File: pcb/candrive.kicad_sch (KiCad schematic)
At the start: 64 parts, among them J1 Conn_01x02_Male, J2 Conn_01x06_Male, J3 Conn_01x06_Male, J4 Conn_01x06_Male, J5 Conn_01x03_Male, J6 Conn_01x06_Male, Q1 AO3401A, Q2 BC546, SW1 SW_Push, U1 STM32F103RBTx, U2 LD1117S33TR_SOT223, U3 SN65HVD234, U6 MAX5035BUSA

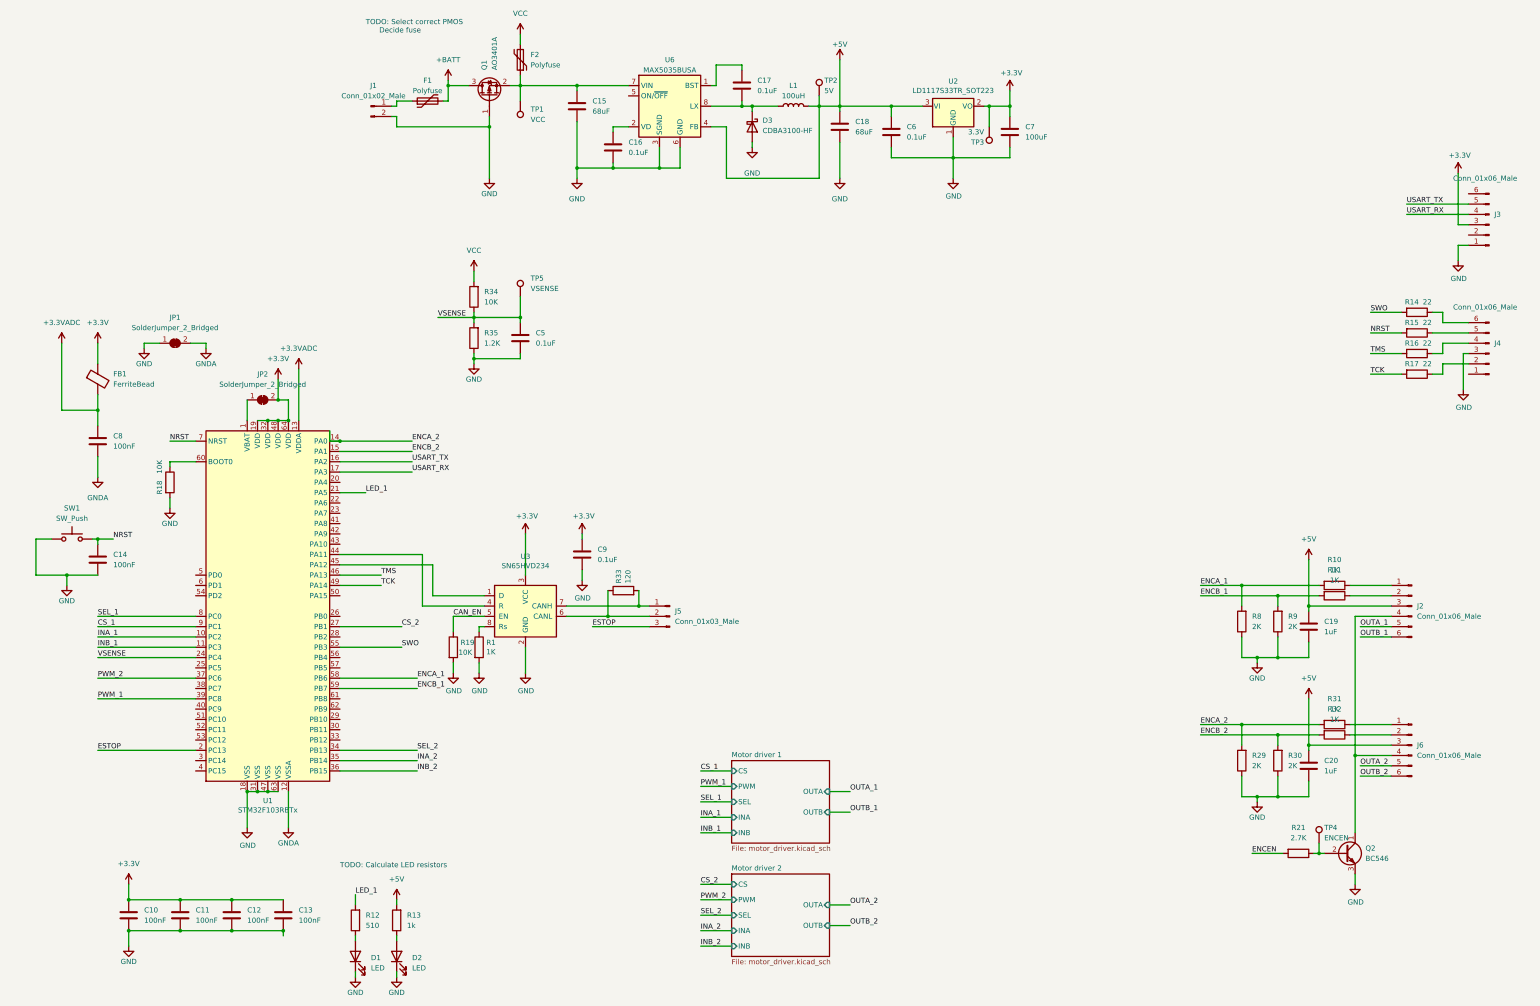
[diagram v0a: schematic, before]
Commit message: Fix some ERC warnings
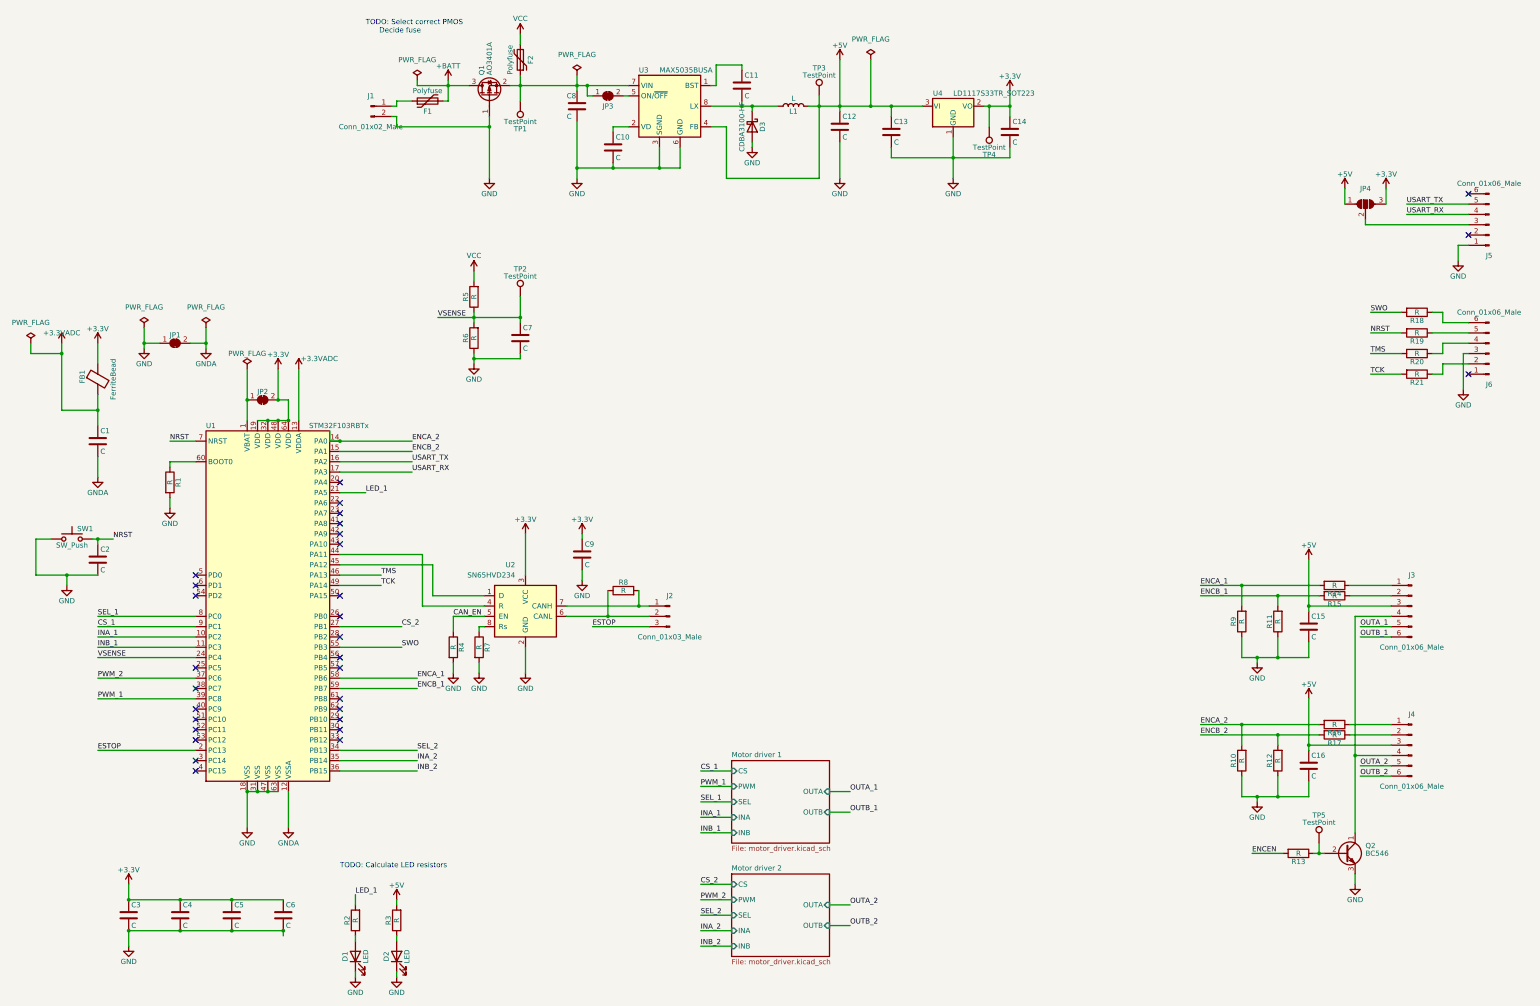
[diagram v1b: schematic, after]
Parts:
- added JP3: SolderJumper_2_Bridged, Jumper:SolderJumper-2_P1.3mm_Open_TrianglePad1.0x1.5mm, symbol Jumper:SolderJumper_2_Bridged
- added JP4: SolderJumper_3_Open, symbol Jumper:SolderJumper_3_Open
- C1: renamed from C8; value 100nF -> C
- C10: renamed from C16; value 0.1uF -> C
- C11: renamed from C17; value 0.1uF -> C
- C12: renamed from C18; value 68uF -> C
- C13: renamed from C6; value 0.1uF -> C
- C14: renamed from C7; value 100uF -> C
- C15: renamed from C19; value 1uF -> C
- C16: renamed from C20; value 1uF -> C
- C2: renamed from C14; value 100nF -> C
- C3: renamed from C10; value 100nF -> C
- C4: renamed from C11; value 100nF -> C
- C5: renamed from C12; value 100nF -> C
- C6: renamed from C13; value 100nF -> C
- C7: renamed from C5; value 0.1uF -> C
- C8: renamed from C15; value 68uF -> C
- C9: value 0.1uF -> C
- JP2: now left out of the parts list
- L1: value 100uH -> L
- R1: renamed from R18; value 10K -> R
- R10: renamed from R29; value 2K -> R
- R11: renamed from R9; value 2K -> R
- R12: renamed from R30; value 2K -> R
- R13: renamed from R21; value 2.7K -> R
- R14: renamed from R10; value 1K -> R
- R15: renamed from R11; value 1K -> R
- R16: renamed from R31; value 1K -> R
- R17: renamed from R32; value 1K -> R
- R18: renamed from R14; value 22 -> R
- R19: renamed from R15; value 22 -> R
- R2: renamed from R12; value 510 -> R
- R20: renamed from R16; value 22 -> R
- R21: renamed from R17; value 22 -> R
- R3: renamed from R13; value 1k -> R
- R4: renamed from R19; value 10K -> R
- R5: renamed from R34; value 10K -> R
- R6: renamed from R35; value 1.2K -> R
- R7: renamed from R1; value 1K -> R
- R8: renamed from R33; value 120 -> R
- R9: renamed from R8; value 2K -> R
- TP1: value VCC -> TestPoint
- TP2: renamed from TP5; value VSENSE -> TestPoint
- TP3: renamed from TP2; value 5V -> TestPoint
- TP4: renamed from TP3; value 3.3V -> TestPoint
- TP5: renamed from TP4; value ENCEN -> TestPoint
- renumbered J5 to J2, J2 to J3, J6 to J4, J3 to J5, J4 to J6, U3 to U2, U6 to U3, U2 to U4
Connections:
- net +5V: now also JP4.1 (A)
- net at C8.1, F2.1, Q1.2 (S)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: now also JP3.1 (A)
- net at U3.5 (ON/~{OFF}): now also JP3.2 (B)
- net +3V3 renamed +3.3V
- net +3.3V: now also JP4.3 (B); no longer J5.3 (Pin_3)
- new net: J5.3 (Pin_3), JP4.2 (C)
- no-connect marks 0 -> 30

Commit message: Replace VNH7070BAS with TLE7209 in schematic
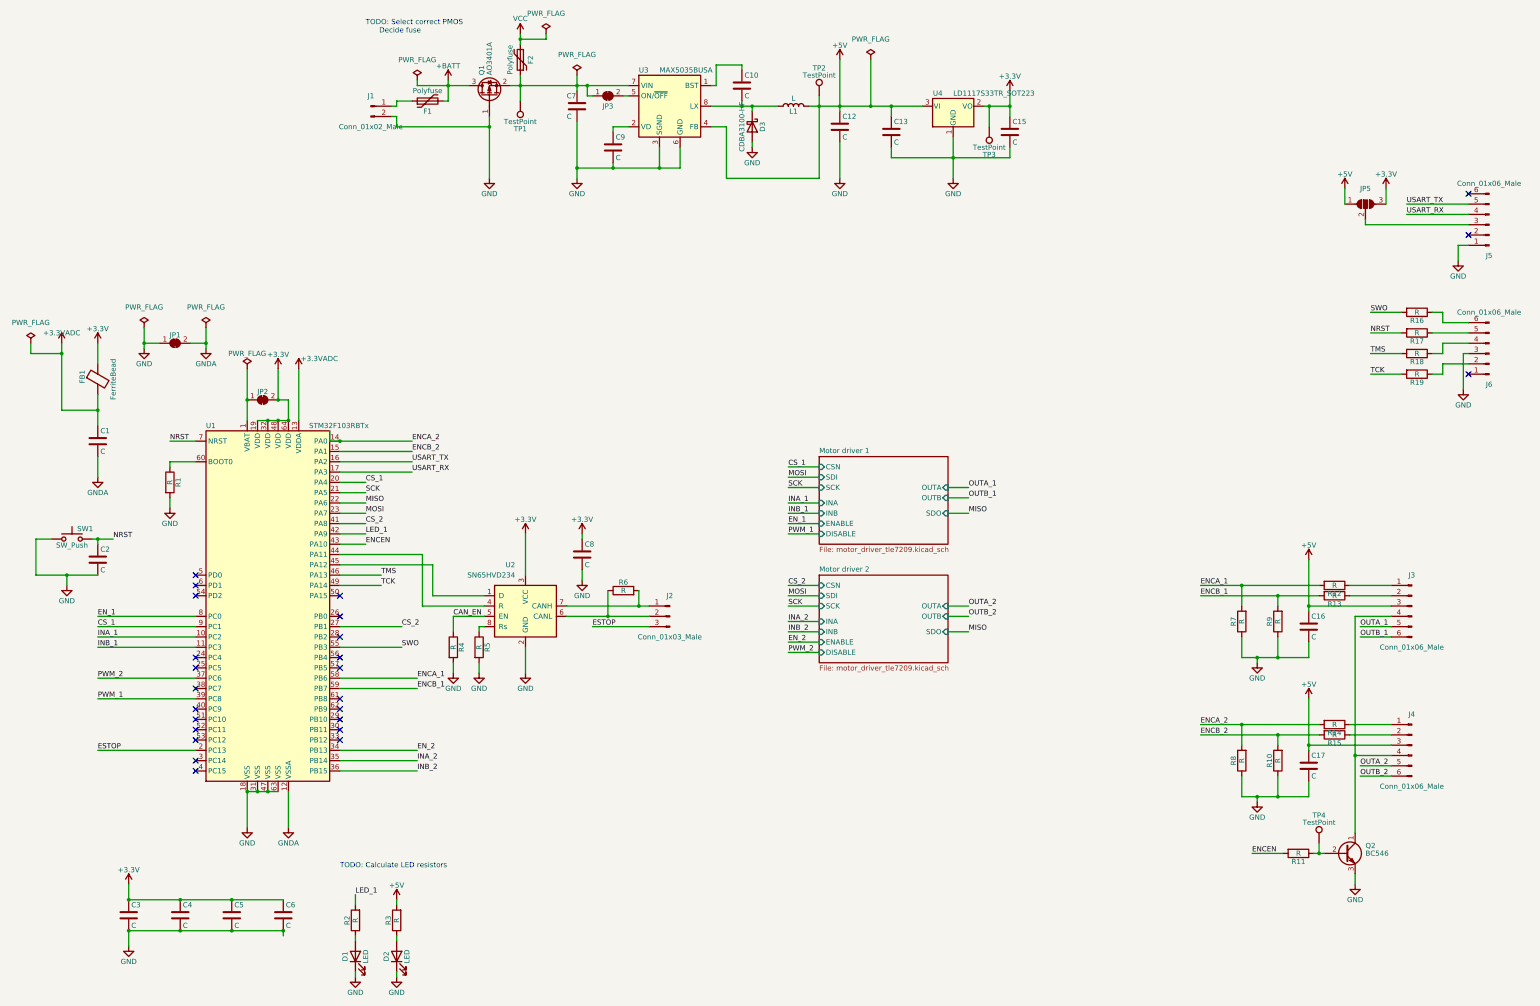
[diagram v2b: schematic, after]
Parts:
- removed C7: C, Capacitor_SMD:C_0805_2012Metric_Pad1.18x1.45mm_HandSolder, symbol Device:C
- removed R5, R6: R, Resistor_SMD:R_0805_2012Metric_Pad1.20x1.40mm_HandSolder, symbol Device:R
- removed TP2: TestPoint, TestPoint:TestPoint_THTPad_D1.0mm_Drill0.5mm, symbol Connector:TestPoint
- renumbered C11 to C10, C14 to C15, C15 to C16, C16 to C17, C8 to C7, C9 to C8, C10 to C9, JP4 to JP5, R12 to R10, R13 to R11, R14 to R12, R15 to R13, R16 to R14, R17 to R15, R18 to R16, R19 to R17, R20 to R18, R21 to R19, R7 to R5, R8 to R6, R9 to R7, R10 to R8, R11 to R9, TP3 to TP2, TP4 to TP3, TP5 to TP4
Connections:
- net CS_1: now also U1.20 (PA4)
- net CS_2: now also U1.41 (PA8)
- net ENCEN: now also U1.43 (PA10)
- net LED_1: now also U1.42 (PA9); no longer U1.21 (PA5)
- net MISO: now reaches U1.22 (PA6)
- net MOSI: now reaches U1.23 (PA7)
- net SEL_1 renamed EN_1
- net SEL_2 renamed EN_2
- net VSENSE: no longer names the net of U1.24 (PC4)
- new net SCK: U1.21 (PA5)
- no-connect marks 30 -> 25
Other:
- sheet Motor driver 1: file motor_driver.kicad_sch -> motor_driver_tle7209.kicad_sch
- sheet Motor driver 1 ports: added CSN, DISABLE, ENABLE, SCK, SDI, SDO; removed CS, PWM, SEL
- sheet Motor driver 2: file motor_driver.kicad_sch -> motor_driver_tle7209.kicad_sch
- sheet Motor driver 2 ports: added CSN, DISABLE, ENABLE, SCK, SDI, SDO; removed CS, PWM, SEL

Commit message: Add missing footprint
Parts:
- JP5: footprint (none) -> Jumper:SolderJumper-3_P2.0mm_Open_TrianglePad1.0x1.5mm
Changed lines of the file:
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@@
       (effects (font (size 1.27 1.27)) hide)
     )
-    (property "Footprint" "" (id 2) (at 353.06 67.31 0)
+    (property "Footprint" "Jumper:SolderJumper-3_P2.0mm_Open_TrianglePad1.0x1.5mm" (id 2) (at 353.06 67.31 0)
       (effects (font (size 1.27 1.27)) hide)
     )
@@
     )
     (path "/9004a9a0-5a74-478c-a0b9-f7a74eb92eb6"
-      (reference "JP5") (unit 1) (value "SolderJumper_3_Open") (footprint "")
+      (reference "JP5") (unit 1) (value "SolderJumper_3_Open") (footprint "Jumper:SolderJumper-3_P2.0mm_Open_TrianglePad1.0x1.5mm")
     )
     (path "/0faae124-e803-4260-a5b6-c24fa6f1d91e/d35675bd-34fc-4071-a786-583eaa3b55e1"
-      (reference "JP6") (unit 1) (value "SolderJumper_3_Bridged12") (footprint "")
+      (reference "JP6") (unit 1) (value "SolderJumper_3_Bridged12") (footprint "Jumper:SolderJumper-3_P2.0mm_Open_TrianglePad1.0x1.5mm")
     )
     (path "/97b9cf33-6b7f-4257-9ecd-e147ca8f6509/d35675bd-34fc-4071-a786-583eaa3b55e1"
-      (reference "JP7") (unit 1) (value "SolderJumper_3_Bridged12") (footprint "")
+      (reference "JP7") (unit 1) (value "SolderJumper_3_Bridged12") (footprint "Jumper:SolderJumper-3_P2.0mm_Open_TrianglePad1.0x1.5mm")
     )
     (path "/625fea47-5bab-4405-abf6-a7f68cc6d801"
